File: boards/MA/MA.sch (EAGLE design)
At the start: 11 parts

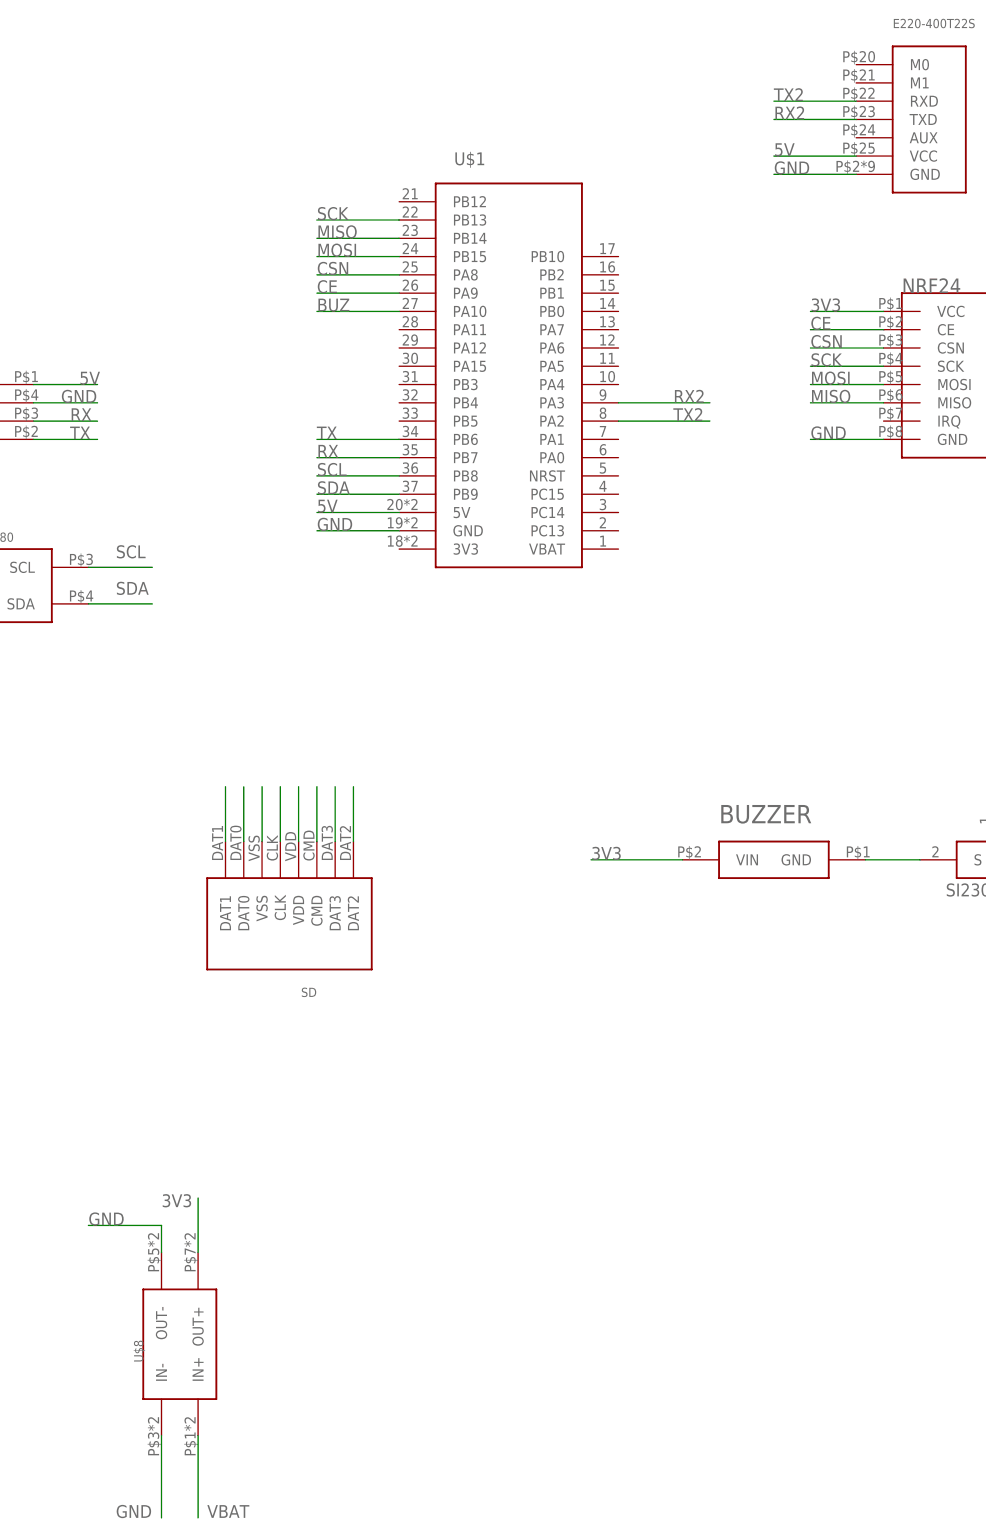
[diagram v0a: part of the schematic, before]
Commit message: Я СДЕЛАЛ ПЛАТЫ С ВРОДЕ НОРМ РАСПИНОВКОЙ И ПОДКЛЮЧЕНИЯМИ . ЕСТЬ ВСЁ КРОМЕ ФОТОРЕЗИСТОРА И ДС-ДС НА 5 ВОЛЬТ
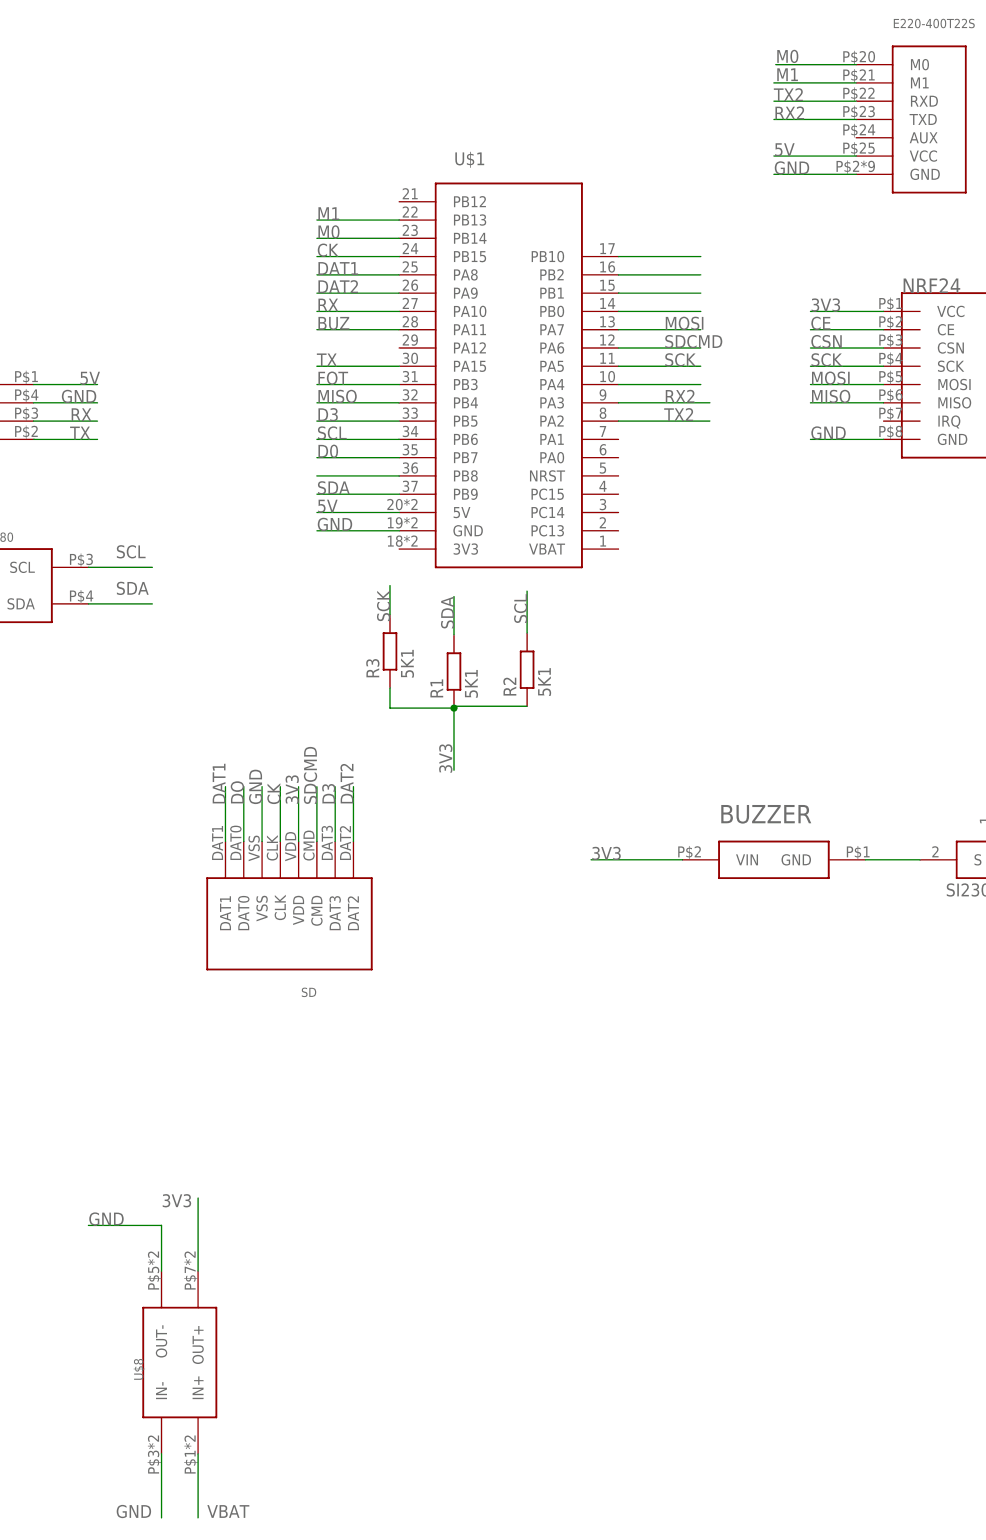
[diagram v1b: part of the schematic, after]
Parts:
- added R1, R2, R3: 5K1, rcl:R-EU_R0603
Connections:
- net N$9 renamed DO
- removed net N$10: SD.DAT2
- removed net N$4: SD.VDD
- new net CK: SD.CLK, U$1.PB15
- new net D0: U$1.PB7
- new net D3: SD.DAT3, U$1.PB5
- new net DAT1: SD.DAT1, U$1.PA8
- new net DAT2: SD.DAT2, U$1.PA9
- new net FOT: U$1.PB3
- new net M0: E220-400T22S.M0, U$1.PB14
- new net M1: E220-400T22S.M1, U$1.PB13
- new net SDCMD: SD.CMD, U$1.PA6
- net 3V3: now also R1.1, R2.1, R3.1, SD.VDD
- net BUZ: now also U$1.PA11; no longer U$1.PA10
- net CE: no longer U$1.PA9
- net CSN: no longer U$1.PA8
- net GND: now also SD.VSS
- net MISO: now also U$1.PB4; no longer U$1.PB14
- net MOSI: now also U$1.PA7; no longer U$1.PB15
- net N$1: now also U$1.PB10; no longer SD.VSS
- net N$5: now also U$1.PB0; no longer SD.CLK
- net N$6: now also U$1.PB1; no longer SD.CMD
- net N$7: now also U$1.PB2; no longer SD.DAT3
- net N$8: now also U$1.PA4; no longer SD.DAT1
- net RX: now also U$1.PA10; no longer U$1.PB7
- net SCK: now also R3.2, U$1.PA5; no longer U$1.PB13
- net SCL: now also R2.2, U$1.PB6
- net SDA: now also R1.2
- net TX: now also U$1.PA15; no longer U$1.PB6
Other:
- moved on the sheet: U$8

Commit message: доделал платы до приемлемого уровня.
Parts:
- added BURNER, FOTOREZ, JP1, JP3: (no value), pinhead:PINHD-1X2
- added LED2: (no value), led:LEDCHIP-LED0603
- added R4, R6, R8, R9: 10K, rcl:R-EU_R0603
- added R5, R7: 100R, rcl:R-EU_R0603
- added U$3: SI2302CDS, CanCubeSat:SI2302CDS
- added U$4: MP1584-B, UNKNOWN-2024:MP1584-B
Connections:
- removed net N$1: U$1.PB10
- removed net N$5: U$1.PB0
- removed net N$6: U$1.PB1
- removed net N$7: U$1.PB2
- removed net N$8: U$1.PA4
- new net AUX: LED2.C, U$1.PB2
- new net IRQ: NRF24.IRQ, U$1.PB10
- new net N$4: E220-400T22S.AUX, R8.2
- new net N$9: LED2.A, R8.1
- new net PRJ: R7.2, U$1.PA4
- net 3V3: now also FOTOREZ.1
- net 5V: now also U$4.OUT+
- net BUZ: now also R4.1, R5.1, R5.2, R6.1, R7.1, U$3.G
- net FOT: now also FOTOREZ.2, R9.2, U$1.PB0, U$1.PB1
- net GND: now also JP1.2, R4.2, R6.2, R9.1, U$2.D, U$3.D, U$4.IN-, U$4.OUT-
- net N$3: now also JP3.1, U$3.S; no longer U$2.D
- net VBAT: now also JP1.1, JP3.2, U$4.IN+
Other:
- moved on the sheet: BME280, BUZZER, E220-400T22S, LIS3MDL, LSM6DSLTR, NEO8M, NRF24, R1, R2, R3, SD, U$8

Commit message: Сделано система САС ДА . всё .
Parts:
- removed R3: 5K1, rcl:R-EU_R0603
- R8, R9: value 10K -> 2K
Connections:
- removed net N$3: JP3.1, U$3.S
- removed net N$4: E220-400T22S.AUX, R8.2
- new net N$1: BUZZER.GND, U$2.D
- net 3V3: no longer R3.1
- net AUX: now also E220-400T22S.AUX, R8.2, U$1.PA4; no longer LED2.C, U$1.PB2
- net CE: now also U$1.PB12
- net CSN: now also U$1.PB13
- net FOT: no longer U$1.PB0, U$1.PB3
- net GND: now also LED2.C, U$2.S, U$3.S; no longer U$2.D, U$3.D
- net IRQ: now also U$1.PB14; no longer U$1.PB10
- net M0: now also U$1.PA0; no longer U$1.PB14
- net M1: now also U$1.PA1; no longer U$1.PB13
- net N$2: now also JP3.1, U$3.D; no longer BUZZER.GND, U$2.S
- net PRJ: now also U$1.PB10; no longer U$1.PA4
- net SCK: no longer R3.2
- net SCL: no longer U$1.PB6
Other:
- moved on the sheet: BURNER, R4, R5, R6, R7

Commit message: матка на проверку .
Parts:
- removed JP1, JP3: (no value), pinhead:PINHD-1X2
- removed U$8: MP1584-B, UNKNOWN-2024:MP1584-B
- added AB: (no value), pinhead:PINHD-1X2
- added BLACKPILL: STM32F411_BOARD, MA:STM32F411_BOARD
- added DCDC-3: MP1584-B, UNKNOWN-2024:MP1584-B
- added LED1: (no value), led:LEDCHIP-LED0603
- added R3: 2K, rcl:R-EU_R0603
- U$1: value STM32F411_BOARD -> DS-DS_5V; device MA:STM32F411_BOARD -> MA:DS-DS_5V
- U$4: value MP1584-B -> SWITCH_MSS; device UNKNOWN-2024:MP1584-B -> UNKNOWN-2024:SWITCH_MSS
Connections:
- removed net DO: SD.DAT0
- new net N$3: R6.1, R7.1, U$3.G
- new net N$4: R4.1, R5.1, U$2.G
- new net N$5: LED1.A, U$4.S
- new net N$7: R3.2, U$4.P
- new net SWITCH: BLACKPILL.PB2, U$4.O
- net 3V3: now also DCDC-3.OUT+, R3.1; no longer U$8.OUT+
- net 5V: now also BLACKPILL.5V, U$1.VCC_OUT; no longer U$1.5V, U$4.OUT+
- net AUX: now also BLACKPILL.PA4; no longer U$1.PA4
- net BUZ: now also BLACKPILL.PA11; no longer R4.1, R5.1, R6.1, R7.1, U$1.PA11, U$2.G, U$3.G
- net CE: now also BLACKPILL.PB12; no longer U$1.PB12
- net CK: now also BLACKPILL.PB15; no longer U$1.PB15
- net CSN: now also BLACKPILL.PB13; no longer U$1.PB13
- net D0: now also BLACKPILL.PB7, SD.DAT0; no longer U$1.PB7
- net D3: now also BLACKPILL.PB5; no longer U$1.PB5
- net DAT1: now also BLACKPILL.PA8; no longer U$1.PA8
- net DAT2: now also BLACKPILL.PA9; no longer U$1.PA9
- net FOT: now also BLACKPILL.PB1; no longer U$1.PB1
- net GND: now also AB.2, BLACKPILL.GND, DCDC-3.IN-, DCDC-3.OUT-, LED1.C, U$1.GND_IN, U$1.GND_OUT; no longer JP1.2, U$1.GND, U$4.IN-, U$4.OUT-, U$8.IN-, U$8.OUT-
- net IRQ: now also BLACKPILL.PB14; no longer U$1.PB14
- net M0: now also BLACKPILL.PA0; no longer U$1.PA0
- net M1: now also BLACKPILL.PA1; no longer U$1.PA1
- net MISO: now also BLACKPILL.PB4; no longer U$1.PB4
- net MOSI: now also BLACKPILL.PA7; no longer U$1.PA7
- net N$2: now also BURNER.1; no longer JP3.1
- net PRJ: now also BLACKPILL.PB10; no longer U$1.PB10
- net RX: now also BLACKPILL.PA10; no longer U$1.PA10
- net RX2: now also BLACKPILL.PA3; no longer U$1.PA3
- net SCK: now also BLACKPILL.PA5; no longer U$1.PA5
- net SCL: now also BLACKPILL.PB8; no longer U$1.PB8
- net SDA: now also BLACKPILL.PB9; no longer U$1.PB9
- net SDCMD: now also BLACKPILL.PA6; no longer U$1.PA6
- net TX: now also BLACKPILL.PA15; no longer U$1.PA15
- net TX2: now also BLACKPILL.PA2; no longer U$1.PA2
- net VBAT: now also AB.1, BURNER.2, DCDC-3.IN+, U$1.VCC_IN; no longer JP1.1, JP3.2, U$4.IN+, U$8.IN+
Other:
- note added: "КНПН-С.А2000-0Э3"
- note added: "Команда "КНПН-С""
- note added: "Плата МА"
- note added: "Схема электрическая принципиальная"
- note added: "Э3"
- moved on the sheet: BME280, BURNER, BUZZER, E220-400T22S, FOTOREZ, LED2, LIS3MDL, LSM6DSLTR, NEO8M, NRF24, R1, R2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
